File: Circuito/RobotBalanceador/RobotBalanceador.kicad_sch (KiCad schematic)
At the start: 14 parts, among them J1 Conn_01x04_Pin, SW1 SW_SPDT, U1 STM32F103C8Tx, Y1 8MHz

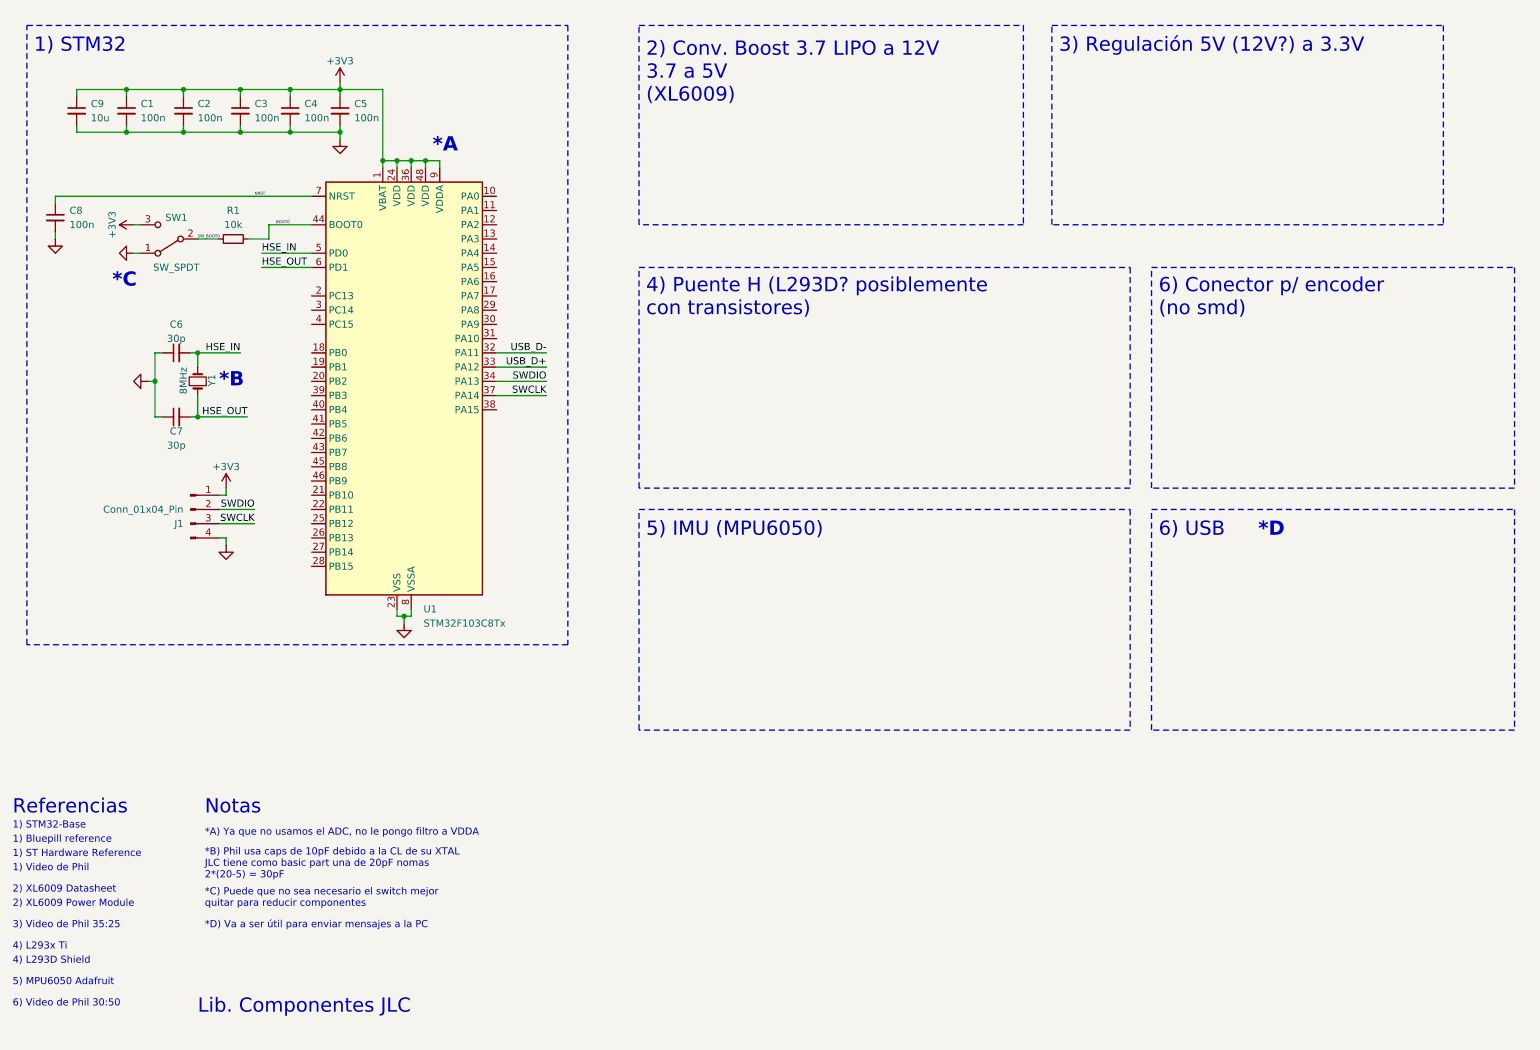
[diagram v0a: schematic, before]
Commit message: Añadido circuitos boost, regulación y USB
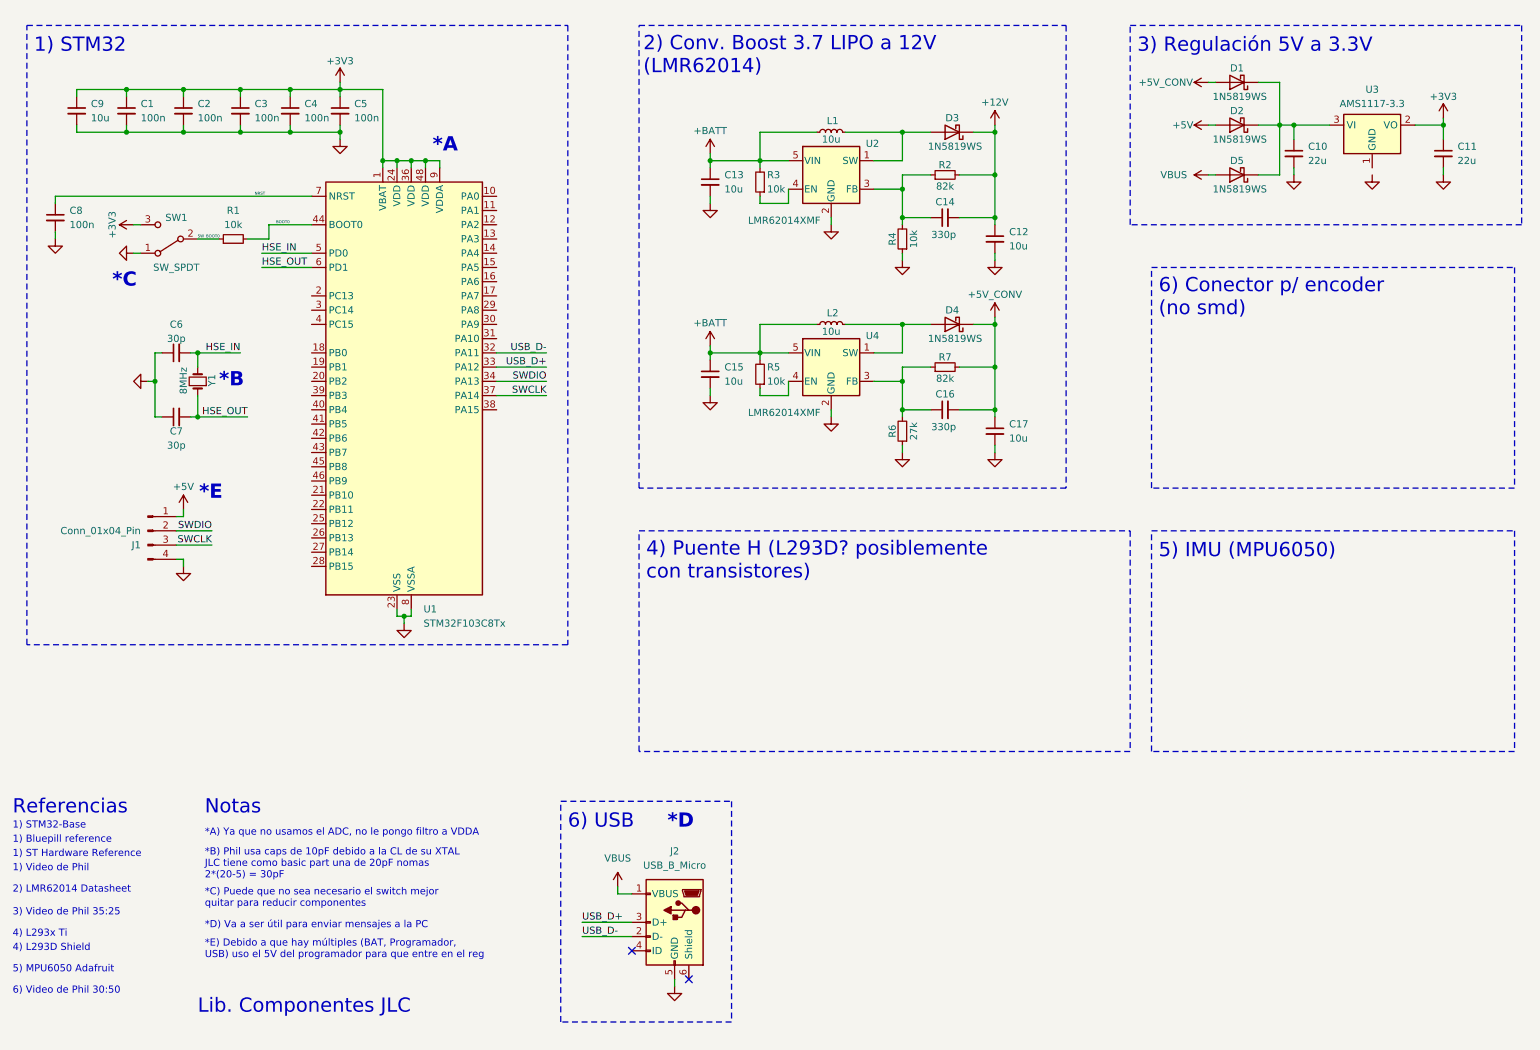
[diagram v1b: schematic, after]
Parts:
- added C10, C11: 22u, Capacitor_SMD:C_0805_2012Metric, symbol Device:C_Small
- added C12, C13, C15, C17: 10u, Capacitor_SMD:C_0603_1608Metric, symbol Device:C_Small
- added C14, C16: 330p, Capacitor_SMD:C_0603_1608Metric, symbol Device:C_Small
- added D1, D2, D3, D4, D5: 1N5819WS, Diode_SMD:D_SOD-323, symbol Diode:1N5819WS
- added J2: USB_B_Micro, Connector_USB:USB_Micro-AB_Molex_47590-0001, symbol Connector:USB_B_Micro
- added L1, L2: 10u, Inductor_SMD:L_1008_2520Metric, symbol Device:L_Small
- added R2, R7: 82k, Resistor_SMD:R_0603_1608Metric, symbol Device:R_Small
- added R3, R4, R5: 10k, Resistor_SMD:R_0603_1608Metric, symbol Device:R_Small
- added R6: 27k, Resistor_SMD:R_0603_1608Metric, symbol Device:R_Small
- added U2, U4: LMR62014XMF, Package_TO_SOT_SMD:SOT-23-5, symbol Regulator_Switching:LMR62014XMF
- added U3: AMS1117-3.3, Package_TO_SOT_SMD:SOT-223-3_TabPin2, symbol Regulator_Linear:AMS1117-3.3
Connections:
- net +3V3: now also C11.1, U3.2 (VO); no longer J1.1 (Pin_1)
- net GND: now also C10.2, C11.2, C12.2, C13.2, C15.2, C17.2, J2.5 (GND), R4.1, R6.1, U2.2 (GND), U4.2 (GND)
- net USB_D+: now also J2.3 (D+)
- net USB_D-: now also J2.2 (D-)
- new net: C10.1, D1.1 (K), D2.1 (K), D5.1 (K), U3.3 (VI)
- new net: D4.2 (A), L2.2, U4.1 (SW)
- new net: C16.1, R6.2, R7.1, U4.3 (FB)
- new net: R5.1, U4.4 (EN)
- new net: D3.2 (A), L1.2, U2.1 (SW)
- new net: C14.1, R2.1, R4.2, U2.3 (FB)
- new net: R3.1, U2.4 (EN)
- new net +12V: C12.1, C14.2, D3.1 (K), R2.2
- new net +5V: D2.2 (A), J1.1 (Pin_1)
- new net +5V_CONV: C16.2, C17.1, D1.2 (A), D4.1 (K), R7.2
- new net +BATT: C13.1, C15.1, L1.1, L2.1, R3.2, R5.2, U2.5 (VIN), U4.5 (VIN)
- new net VBUS: D5.2 (A), J2.1 (VBUS)
- no-connect marks 0 -> 2
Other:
- note added: "*E"
- note added: "*E) Debido a que hay múltiples (BAT, Programador, USB) uso el 5V del programador para que entre en el reg"
- note added: "2) Conv. Boost 3.7 LIPO a 12V (LMR62014)"
- note added: "2) LMR62014 Datasheet"
- note added: "3) Regulación 5V a 3.3V"
- note removed: "2) Conv. Boost 3.7 LIPO a 12V 3.7 a 5V (XL6009)"
- note removed: "2) XL6009 Datasheet"
- note removed: "2) XL6009 Power Module"
- note removed: "3) Regulación 5V (12V?) a 3.3V"
- moved on the sheet: J1

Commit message: Añadido MPU6050
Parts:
- added C18, C20: 100n, Capacitor_SMD:C_0603_1608Metric, symbol Device:C_Small
- added C19: 2.2n, Capacitor_SMD:C_0603_1608Metric, symbol Device:C_Small
- added R8: 10k, Resistor_SMD:R_0603_1608Metric, symbol Device:R_Small
- added U5: MPU-6050, Sensor_Motion:InvenSense_QFN-24_4x4mm_P0.5mm, symbol Sensor_Motion:MPU-6050
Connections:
- net +3V3: now also C20.1, U5.13 (VDD), U5.8 (VLOGIC)
- net GND: now also U3.1 (GND), C18.2, C19.2, C20.2, R8.1, U5.1 (CLKIN), U5.11 (FSYNC), U5.18 (GND)
- new net: R8.2, U5.9 (AD0)
- new net: C18.1, U5.10 (REGOUT)
- new net: C19.1, U5.20 (CPOUT)
- new net MPU6050_INT: U5.12 (INT)
- new net MPU6050_SCL: U5.23 (SCL)
- new net MPU6050_SDA: U5.24 (SDA)
- no-connect marks 2 -> 4
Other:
- note added: "6) Conector p/ encoder(no smd)"
- note removed: "6) Conector p/ encoder (no smd)"
- moved on the sheet: C12, C13, C14, C15, C16, C17, D3, D4, J2, L1, L2, R2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

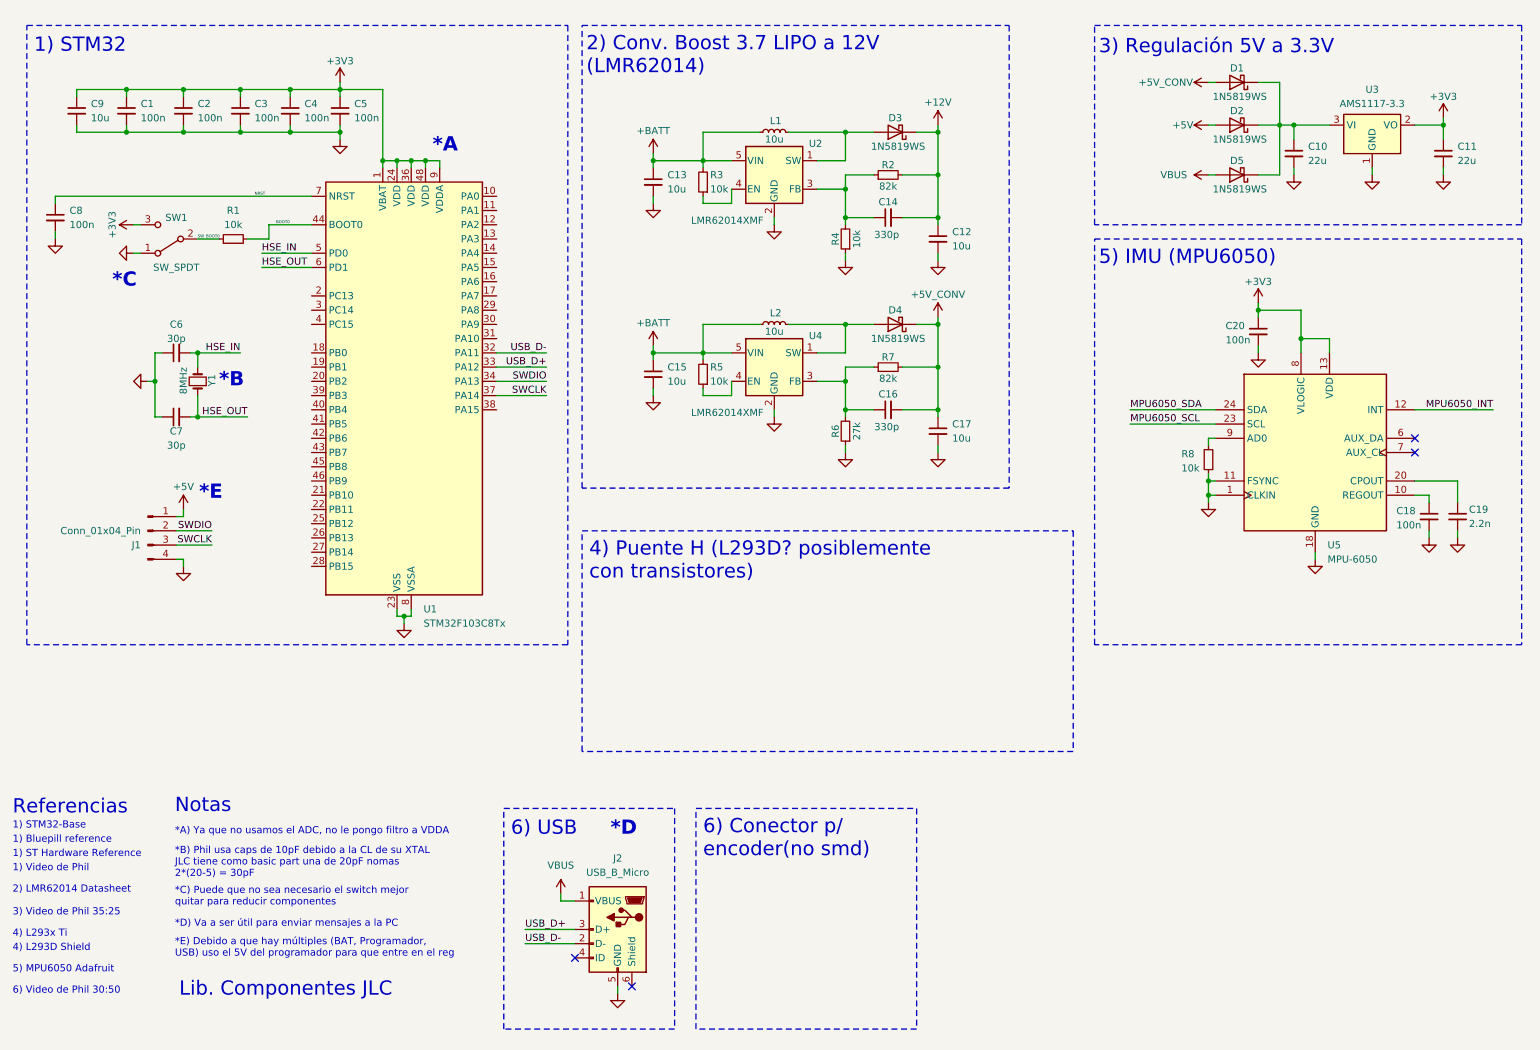
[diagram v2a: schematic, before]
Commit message: Añadido conector para encoder y jack para batería
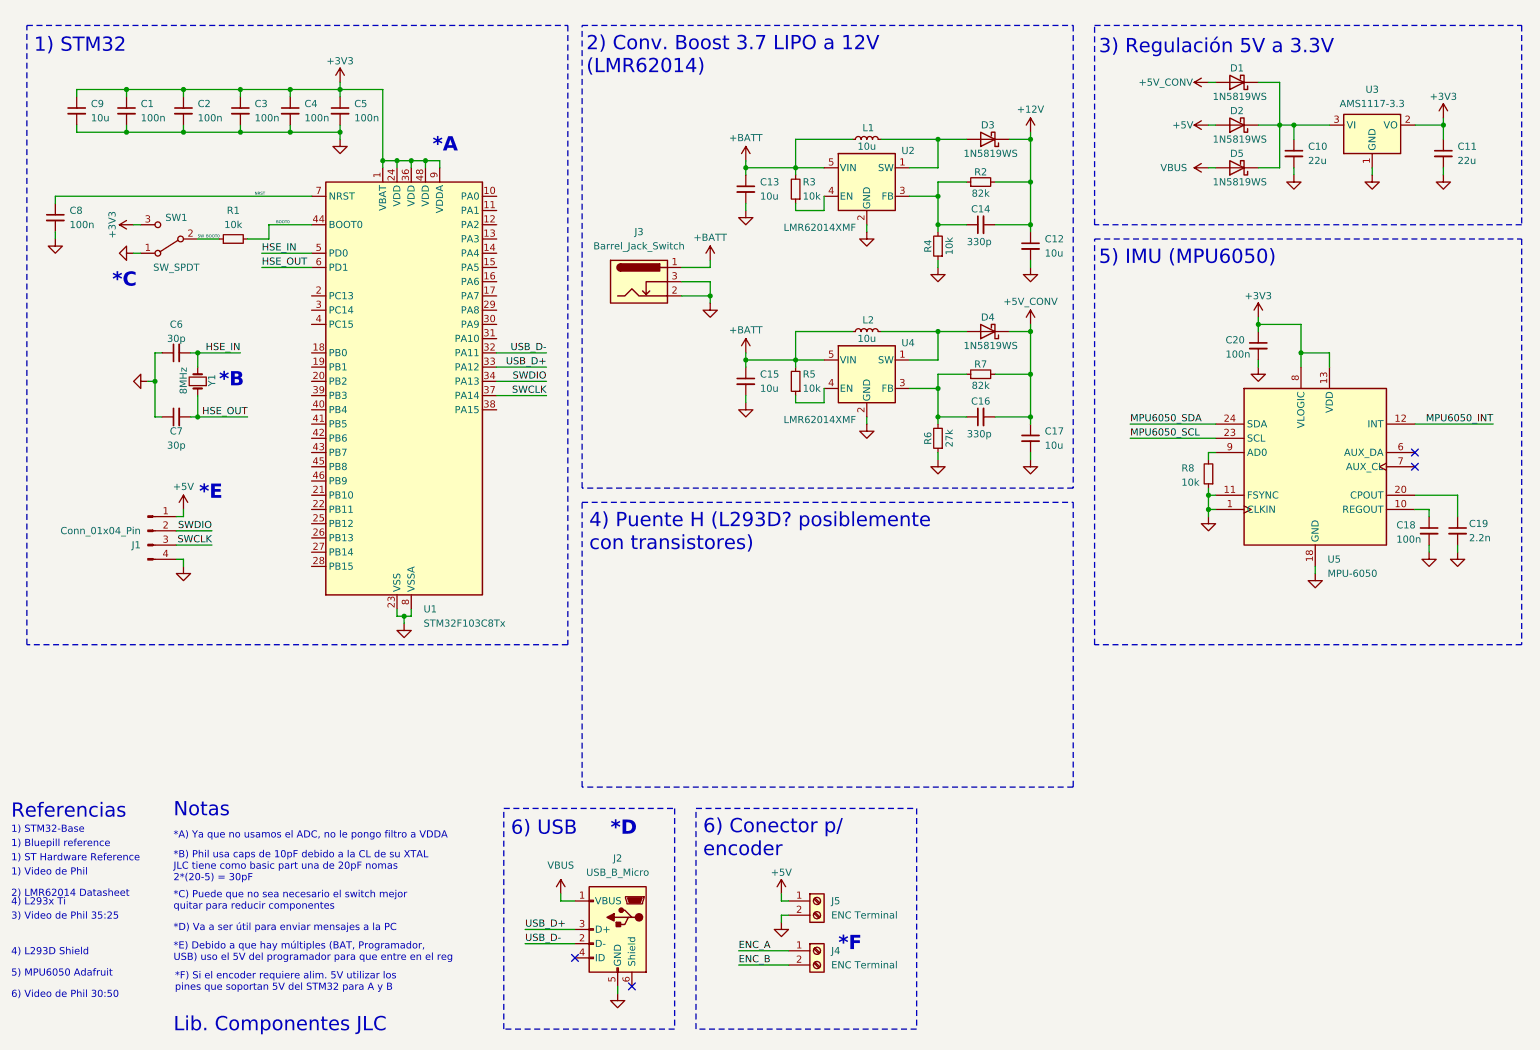
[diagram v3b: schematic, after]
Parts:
- added J3: Barrel_Jack_Switch, Connector_BarrelJack:BarrelJack_GCT_DCJ200-10-A_Horizontal, symbol Connector:Barrel_Jack_Switch
- added J4, J5: ENC Terminal, TerminalBlock:TerminalBlock_bornier-2_P5.08mm, symbol Connector:Screw_Terminal_01x02
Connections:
- net +5V: now also J5.1 (Pin_1)
- net +BATT: now also J3.1
- net GND: now also J3.2, J3.3, J5.2 (Pin_2)
- new net ENC_A: J4.1 (Pin_1)
- new net ENC_B: J4.2 (Pin_2)
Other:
- note added: "*F"
- note added: "*F) Si el encoder requiere alim. 5V utilizar los pines que soportan 5V del STM32 para A y B"
- note added: "6) Conector p/ encoder"
- note removed: "6) Conector p/ encoder(no smd)"
- moved on the sheet: C12, C13, C14, C15, C16, C17, C18, C19, C20, D3, D4, D5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

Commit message: Añadido puente H
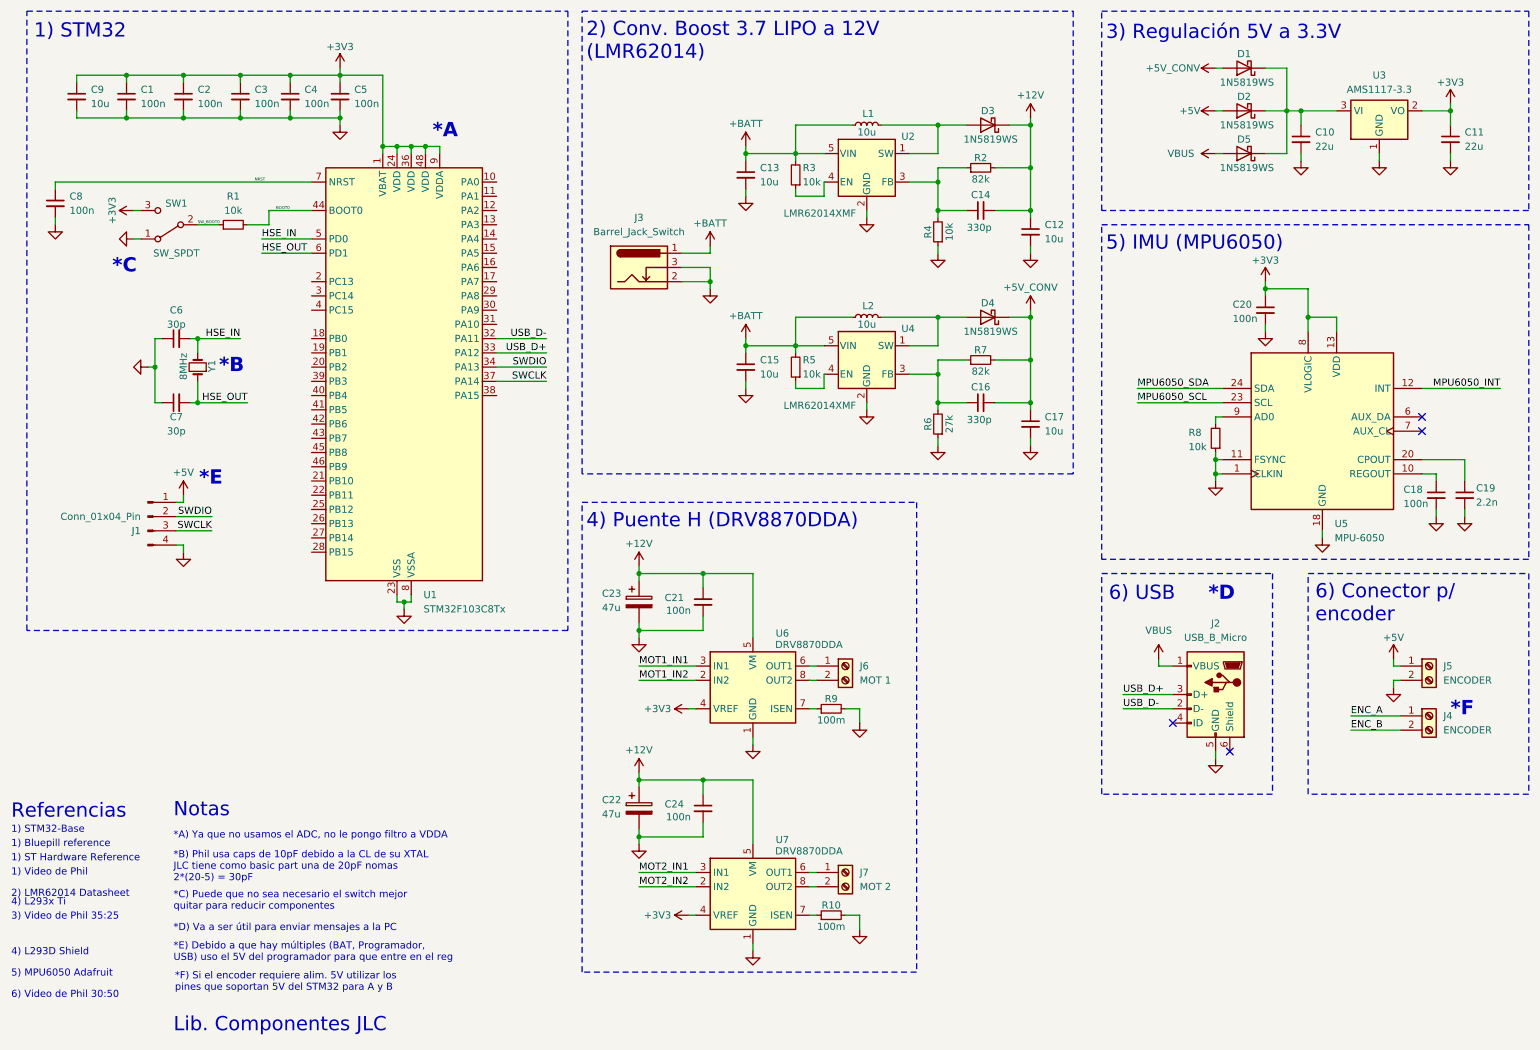
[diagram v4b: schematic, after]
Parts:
- added C21, C24: 100n, Capacitor_SMD:C_0603_1608Metric, symbol Device:C_Small
- added C22, C23: 47u, Capacitor_SMD:CP_Elec_6.3x5.4, symbol Device:C_Polarized
- added J6: MOT 1, TerminalBlock:TerminalBlock_bornier-2_P5.08mm, symbol Connector:Screw_Terminal_01x02
- added J7: MOT 2, TerminalBlock:TerminalBlock_bornier-2_P5.08mm, symbol Connector:Screw_Terminal_01x02
- added R10, R9: 100m, Resistor_SMD:R_1206_3216Metric, symbol Device:R_Small
- added U6, U7: DRV8870DDA, Package_SO:Texas_HTSOP-8-1EP_3.9x4.9mm_P1.27mm_EP2.95x4.9mm_Mask2.4x3.1mm_ThermalVias, symbol Driver_Motor:DRV8870DDA
- J4, J5: value ENC Terminal -> ENCODER
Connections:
- net +12V: now also C21.1, C22.1, C23.1, C24.1, U6.5 (VM), U7.5 (VM)
- net +3V3: now also U6.4 (VREF), U7.4 (VREF)
- net GND: now also C21.2, C22.2, C23.2, C24.2, R10.2, R9.2, U6.1 (GND), U6.9 (GND), U7.1 (GND), U7.9 (GND)
- new net: R10.1, U7.7 (ISEN)
- new net: R9.1, U6.7 (ISEN)
- new net: J6.1 (Pin_1), U6.6 (OUT1)
- new net: J6.2 (Pin_2), U6.8 (OUT2)
- new net: J7.1 (Pin_1), U7.6 (OUT1)
- new net: J7.2 (Pin_2), U7.8 (OUT2)
- new net MOT1_IN1: U6.3 (IN1)
- new net MOT1_IN2: U6.2 (IN2)
- new net MOT2_IN1: U7.3 (IN1)
- new net MOT2_IN2: U7.2 (IN2)
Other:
- note added: "4) Puente H (DRV8870DDA)"
- note removed: "4) Puente H (L293D? posiblemente con transistores)"
- moved on the sheet: C1, C10, C11, C12, C13, C14, C15, C16, C17, C18, C19, C2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
